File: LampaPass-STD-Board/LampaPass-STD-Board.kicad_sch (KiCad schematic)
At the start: 0 parts

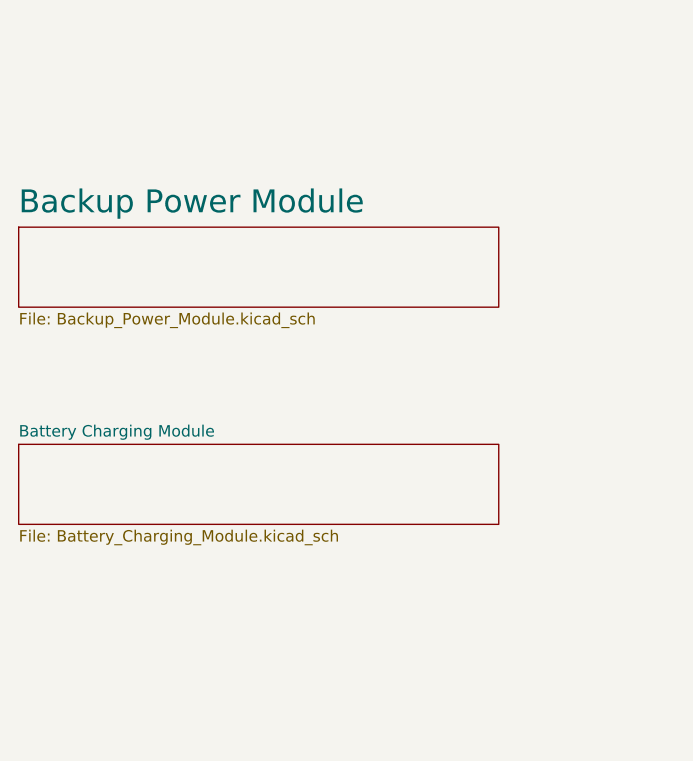
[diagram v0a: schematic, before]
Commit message: Added MCU Peripheral subcircuit. Added TPS2120 datasheet.
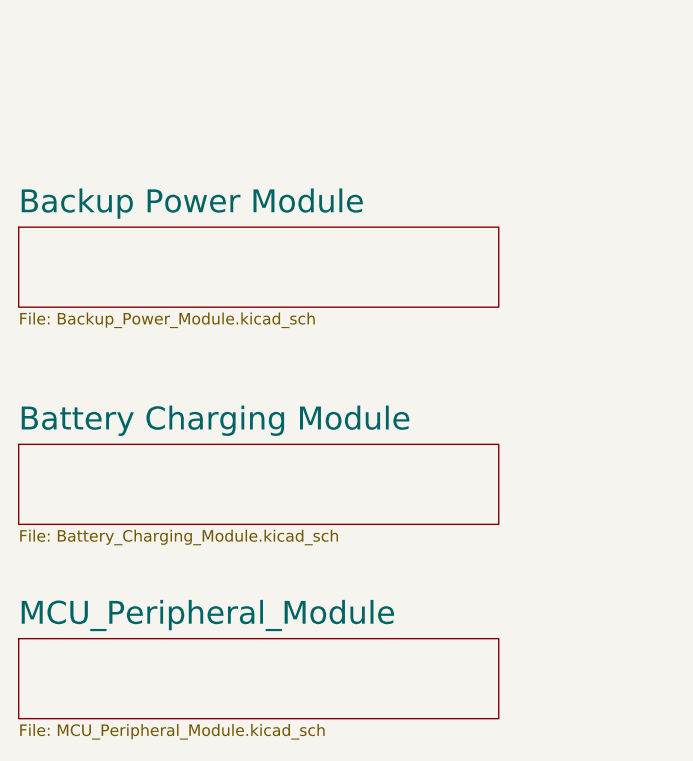
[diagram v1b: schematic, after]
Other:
- added sheet MCU_Peripheral_Module (MCU_Peripheral_Module.kicad_sch)
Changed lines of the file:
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@@
     (stroke (width 0.1524) (type solid))
     (fill (color 255 60 0 1.0000))
-    (property "Sheetname" "Battery Charging Module" (at 120.65 114.8584 0)
-      (effects (font (size 1.27 1.27)) (justify left bottom))
+    (property "Sheetname" "Battery Charging Module" (at 120.65 114.2234 0)
+      (effects (font (size 2.54 2.54)) (justify left bottom))
     )
     (property "Sheetfile" "Battery_Charging_Module.kicad_sch" (at 120.65 125.0446 0)
@@
       )
     )
+  )
+  (sheet (at 120.65 137.16) (size 53.34 8.89) (fields_autoplaced)
+    (stroke (width 0.1524) (type solid))
+    (fill (color 223 255 12 1.0000))
+    (property "Sheetname" "MCU_Peripheral_Module" (at 120.65 135.8134 0)
+      (effects (font (size 2.54 2.54)) (justify left bottom))
+    )
+    (property "Sheetfile" "MCU_Peripheral_Module.kicad_sch" (at 120.65 146.6346 0)
+      (effects (font (size 1.27 1.27)) (justify left top))
+    )
+    (instances
+      (project "LampaPass-STD-Board"
+        (path "/40e9029c-44bc-48bf-a2b7-1f2f10ba39ad" (page "4"))
+      )
+    )

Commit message: Added raw backup power schematic. Merged backup power schematic with battery charging schematic.
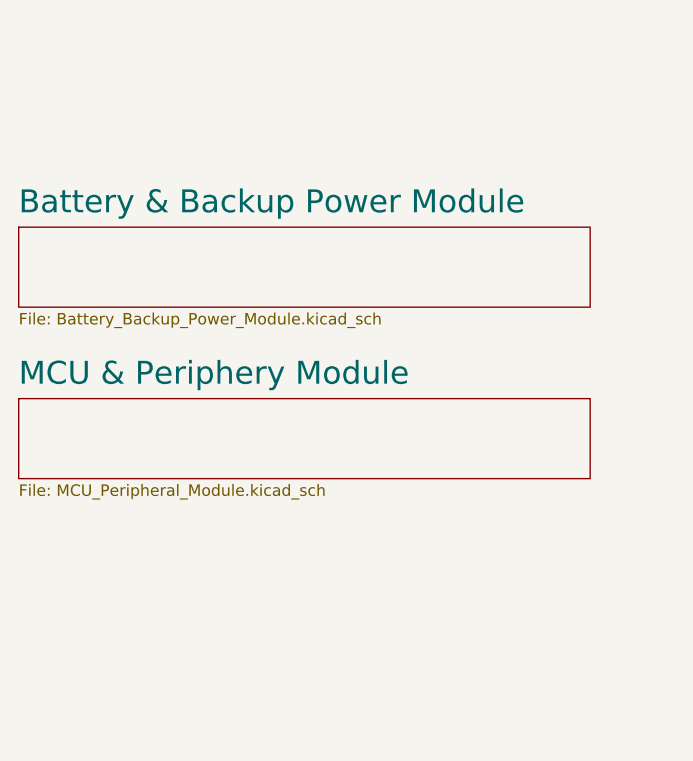
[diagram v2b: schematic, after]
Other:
- sheet Backup Power Module renamed Battery & Backup Power Module
- sheet MCU_Peripheral_Module renamed MCU & Periphery Module
- removed sheet Battery Charging Module
- sheet Battery & Backup Power Module: file Backup_Power_Module.kicad_sch -> Battery_Backup_Power_Module.kicad_sch
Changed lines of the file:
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@@
 (kicad_sch (version 20230121) (generator eeschema)
   (paper "A4")
-  (sheet (at 120.65 115.57) (size 53.34 8.89) (fields_autoplaced)
+  (sheet (at 120.65 110.49) (size 63.5 8.89) (fields_autoplaced)
     (stroke (width 0.1524) (type solid))
-    (fill (color 255 60 0 1.0000))
-    (property "Sheetname" "Battery Charging Module" (at 120.65 114.2234 0)
+    (fill (color 223 255 12 1.0000))
+    (property "Sheetname" "MCU & Periphery Module" (at 120.65 109.1434 0)
       (effects (font (size 2.54 2.54)) (justify left bottom))
     )
-    (property "Sheetfile" "Battery_Charging_Module.kicad_sch" (at 120.65 125.0446 0)
-      (effects (font (size 1.27 1.27)) (justify left top))
-    )
-    (instances
-      (project "LampaPass-STD-Board"
-        (path "/40e9029c-44bc-48bf-a2b7-1f2f10ba39ad" (page "3"))
-      )
-    )
-  )
-  (sheet (at 120.65 137.16) (size 53.34 8.89) (fields_autoplaced)
-    (stroke (width 0.1524) (type solid))
-    (fill (color 223 255 12 1.0000))
-    (property "Sheetname" "MCU_Peripheral_Module" (at 120.65 135.8134 0)
-      (effects (font (size 2.54 2.54)) (justify left bottom))
-    )
-    (property "Sheetfile" "MCU_Peripheral_Module.kicad_sch" (at 120.65 146.6346 0)
+    (property "Sheetfile" "MCU_Peripheral_Module.kicad_sch" (at 120.65 119.9646 0)
       (effects (font (size 1.27 1.27)) (justify left top))
     )
@@
     )
   )
-  (sheet (at 120.65 91.44) (size 53.34 8.89) (fields_autoplaced)
+  (sheet (at 120.65 91.44) (size 63.5 8.89) (fields_autoplaced)
     (stroke (width 0.1524) (type solid))
     (fill (color 255 8 88 1.0000))
-    (property "Sheetname" "Backup Power Module" (at 120.65 90.0934 0)
+    (property "Sheetname" "Battery & Backup Power Module" (at 120.65 90.0934 0)
       (effects (font (size 2.54 2.54)) (justify left bottom))
     )
-    (property "Sheetfile" "Backup_Power_Module.kicad_sch" (at 120.65 100.9146 0)
+    (property "Sheetfile" "Battery_Backup_Power_Module.kicad_sch" (at 120.65 100.9146 0)
       (effects (font (size 1.27 1.27)) (justify left top))
     )

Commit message: Added Battery Backup Power Module. Added Power Mangement empty schematic.
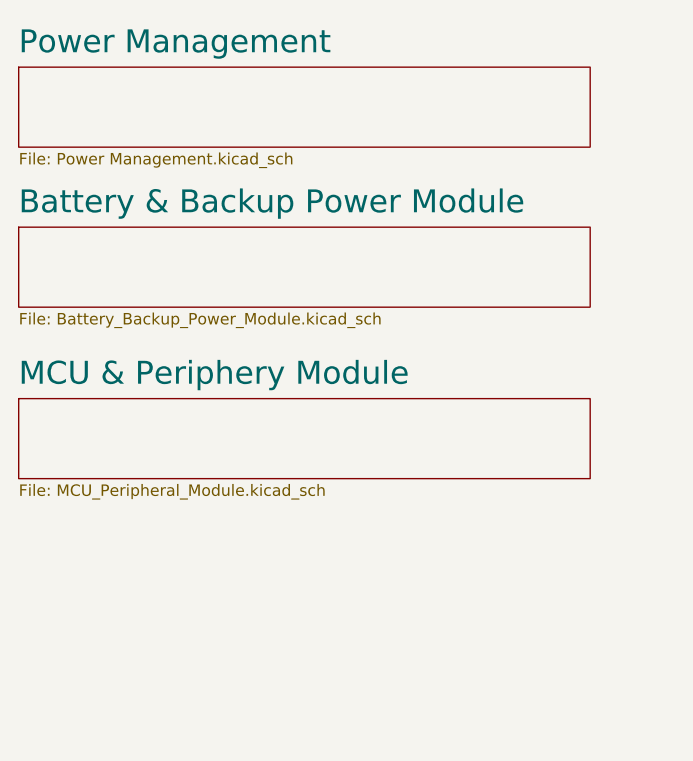
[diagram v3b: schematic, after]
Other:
- added sheet Power Management (Power Management.kicad_sch)
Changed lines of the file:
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@@
 (kicad_sch (version 20230121) (generator eeschema)
   (paper "A4")
+  (sheet (at 120.65 73.66) (size 63.5 8.89) (fields_autoplaced)
+    (stroke (width 0.1524) (type solid))
+    (fill (color 194 0 194 1.0000))
+    (property "Sheetname" "Power Management" (at 120.65 72.3134 0)
+      (effects (font (size 2.54 2.54)) (justify left bottom))
+    )
+    (property "Sheetfile" "Power Management.kicad_sch" (at 120.65 83.1346 0)
+      (effects (font (size 1.27 1.27)) (justify left top))
+    )
+    (instances
+      (project "LampaPass-STD-Board"
+        (path "/40e9029c-44bc-48bf-a2b7-1f2f10ba39ad" (page "4"))
+      )
+    )
+  )
   (sheet (at 120.65 110.49) (size 63.5 8.89) (fields_autoplaced)
     (stroke (width 0.1524) (type solid))
